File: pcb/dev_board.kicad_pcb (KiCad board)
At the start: 6 copper layers, 45.7 x 41.2 mm, 37 parts, among them J1 Conn_02x13_Odd_Even, J2 Conn_02x13_Odd_Even, J4 Conn_01x05, SW1 SW_DIP_x03, SW2 Start, U1 XS-LPC-01, U2 MCP3202, U3 NCP114ASN280T1G, U6 TLV74311

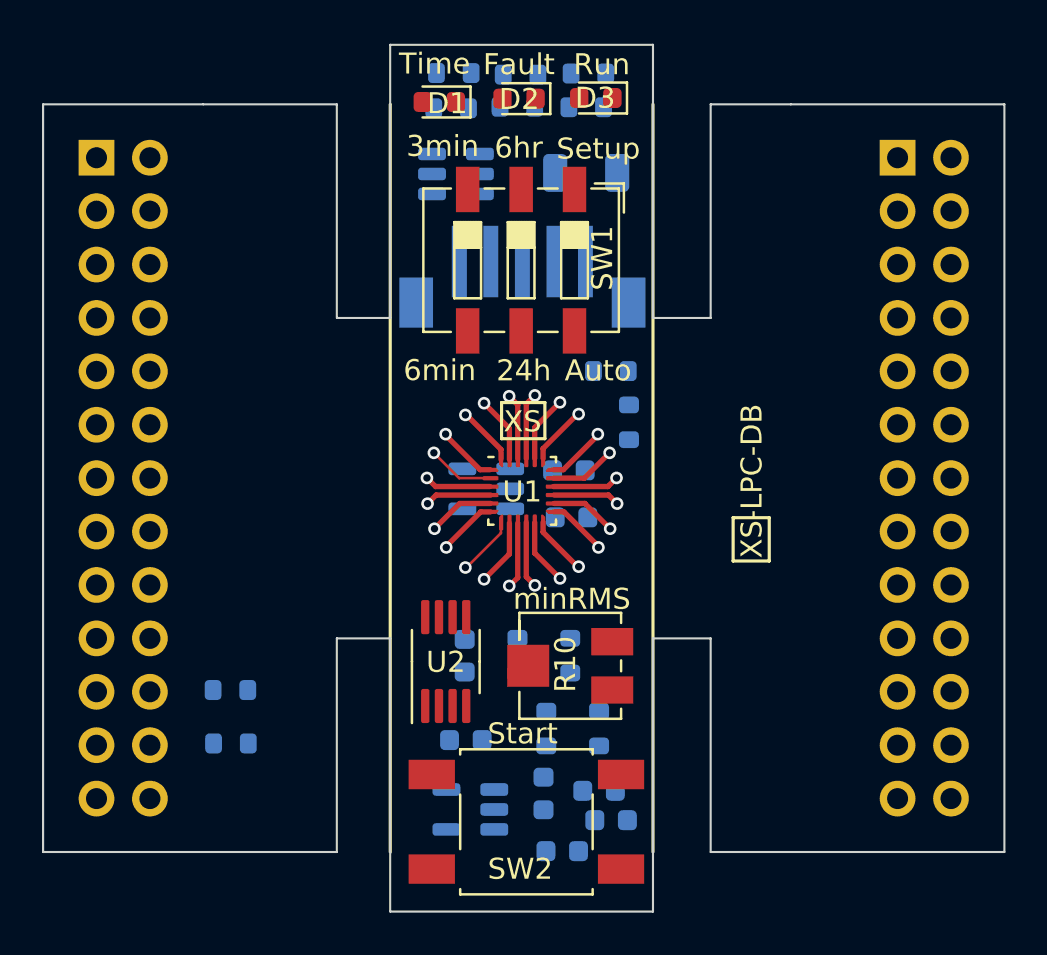
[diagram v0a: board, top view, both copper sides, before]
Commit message: v0.3 emulator winged, clean routed PCB, schem, Digikey BOM. For review and cleanup.
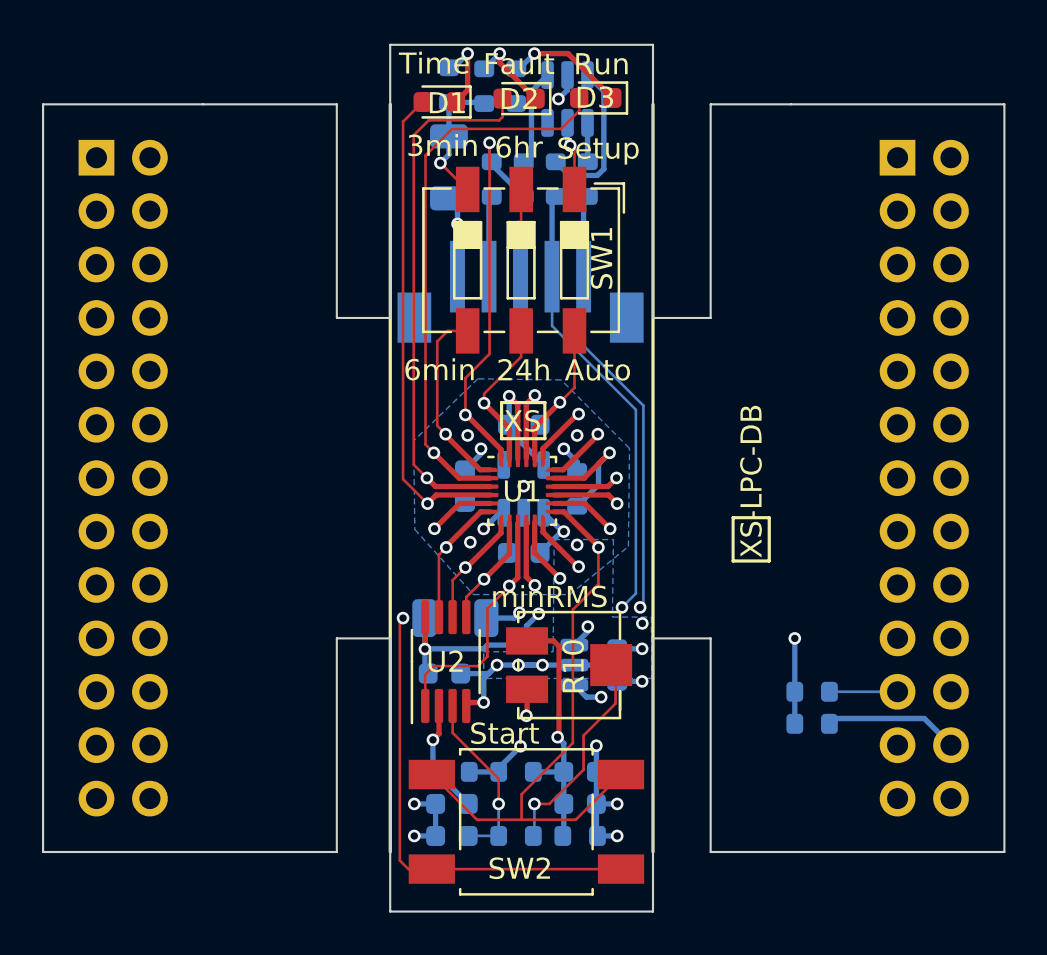
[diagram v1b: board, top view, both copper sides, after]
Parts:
- removed C7: 1u, Capacitor_SMD:C_0603_1608Metric
- added C11: 0.1u, Capacitor_SMD:C_0603_1608Metric, B.Cu at (166.4, 113.4)
- added C12: 10u, Capacitor_SMD:C_1206_3216Metric, B.Cu at (166.9, 110.8)
- added C2: 1u, Capacitor_SMD:C_0603_1608Metric, B.Cu at (167.4, 104.5)
- moved R5 27.7 mm to (183.9, 114.3)
- moved R1 27.7 mm to (183.9, 115.8)
- moved R6 10.7 mm to (168.7, 89.9), turned to -90 degrees
- moved C4 9.23 mm to (174.6, 113.0), turned to 90 degrees
- moved R7 9.08 mm to (172.9, 121.2), turned to 0 degrees
- moved C1 8.94 mm to (172.9, 119.6), turned to 0 degrees
- moved U3 7.85 mm to (171.4, 113.0)
- moved C6 7.61 mm to (166.8, 119.6)
- moved C8 6.53 mm to (166.6, 89.4), turned to 90 degrees
- moved R12 6.46 mm to (169.8, 121.2), turned to 180 degrees
- moved D6 6.39 mm to (172.3, 86.1), turned to 90 degrees
- moved R8 6.10 mm to (169.8, 118.1), turned to 180 degrees
- moved R14 6.01 mm to (171.7, 89.9), turned to -90 degrees
- moved R11 4.94 mm to (166.8, 118.1), turned to 180 degrees
- moved C5 4.61 mm to (166.8, 121.2)
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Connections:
- J1 pad 18: /pump -> Net-(J1-Pin_18)
- J1 pad 6: /run_led -> /setup
- J2 pad 11: /timeout -> /time_led
- J2 pad 13: /time_led -> /fault_led
- J2 pad 15: Net-(J2-Pin_15) -> /run_led
- J2 pad 5: /setup -> /period
- J2 pad 7: /fault_led -> /pump
- J2 pad 9: /period -> /timeout
- U1 pad 1: /period -> /timeout
- U1 pad 14: /pump -> Net-(J1-Pin_18)
- U1 pad 2: /timeout -> /time_led
- U1 pad 20: /run_led -> /setup
- U1 pad 23: /setup -> /period
- U1 pad 24: /fault_led -> /pump
- U1 pad 3: /time_led -> /fault_led
- U1 pad 4: Net-(J2-Pin_15) -> /run_led
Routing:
- net GND: track 2.84 -> 68.6 mm, vias 1 -> 22
- net /start: track 2.84 -> 46.6 mm
- net /time_led: track 3.17 -> 43.9 mm
- net /CT2: track 0.00 -> 40.6 mm, vias 0 -> 2
- net /fault_led: track 2.84 -> 41.9 mm
- net /pump: track 3.17 -> 39.7 mm, vias 1 -> 2
- net /run_led: track 3.17 -> 39.4 mm
- net /CT1: track 0.00 -> 32.8 mm, vias 0 -> 2
- net /adc_ncs: track 3.17 -> 35.0 mm
- net /period: track 2.84 -> 29.4 mm
- net /setup: track 3.17 -> 29.2 mm
- net /timeout: track 3.17 -> 28.0 mm
- net /sleep_n: track 3.17 -> 27.2 mm
- net /adc_mosi: track 3.17 -> 27.0 mm
- net /adc_miso: track 2.84 -> 25.4 mm
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- added copper zone on In4.Cu, net +3.3V
- added copper zone on In4.Cu, net +3V0
- added copper zone on B.Cu, net GND
- added copper zone on In1.Cu, net GND
- added copper zone on In3.Cu, net GND
